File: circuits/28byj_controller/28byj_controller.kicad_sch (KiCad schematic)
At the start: 13 parts, among them J1 INPUT, J2 5V, M1 28BYJ-48_Stepper, M2 28BYJ-48_Stepper, U1 74HC595, U2 ULN2803A

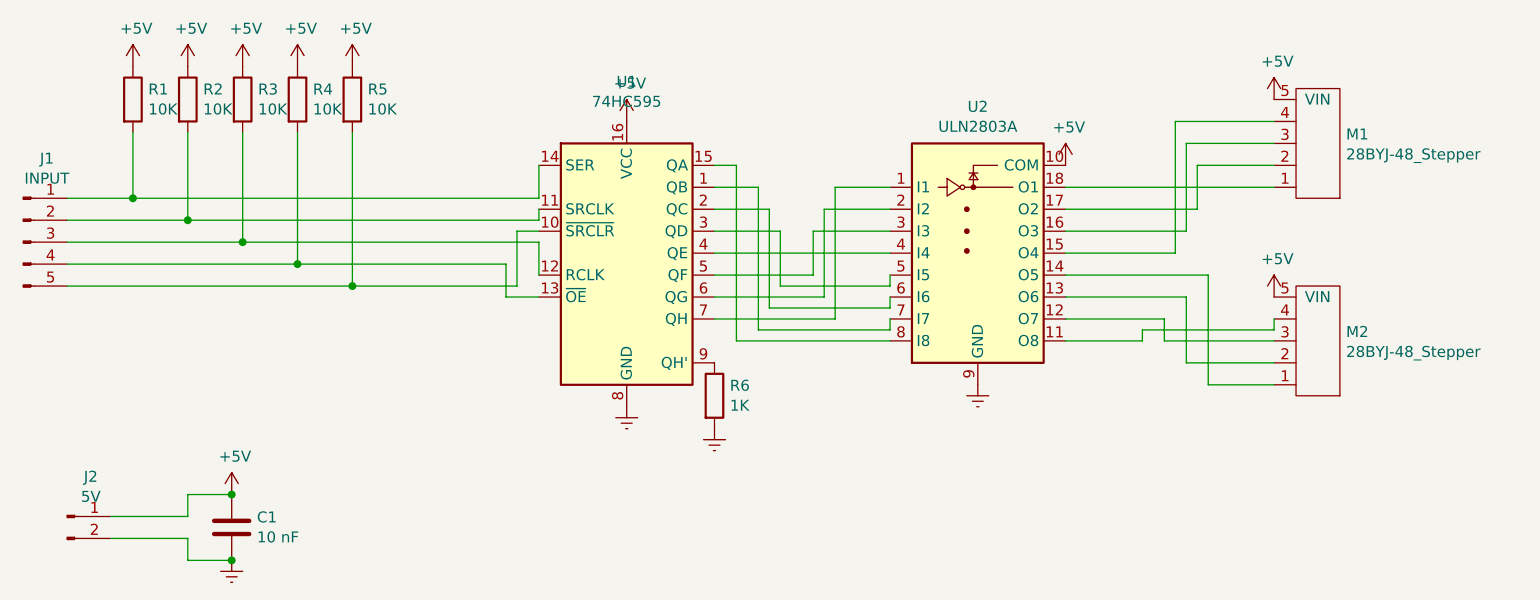
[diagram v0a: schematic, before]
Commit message: Code works and is tested on waveforms.
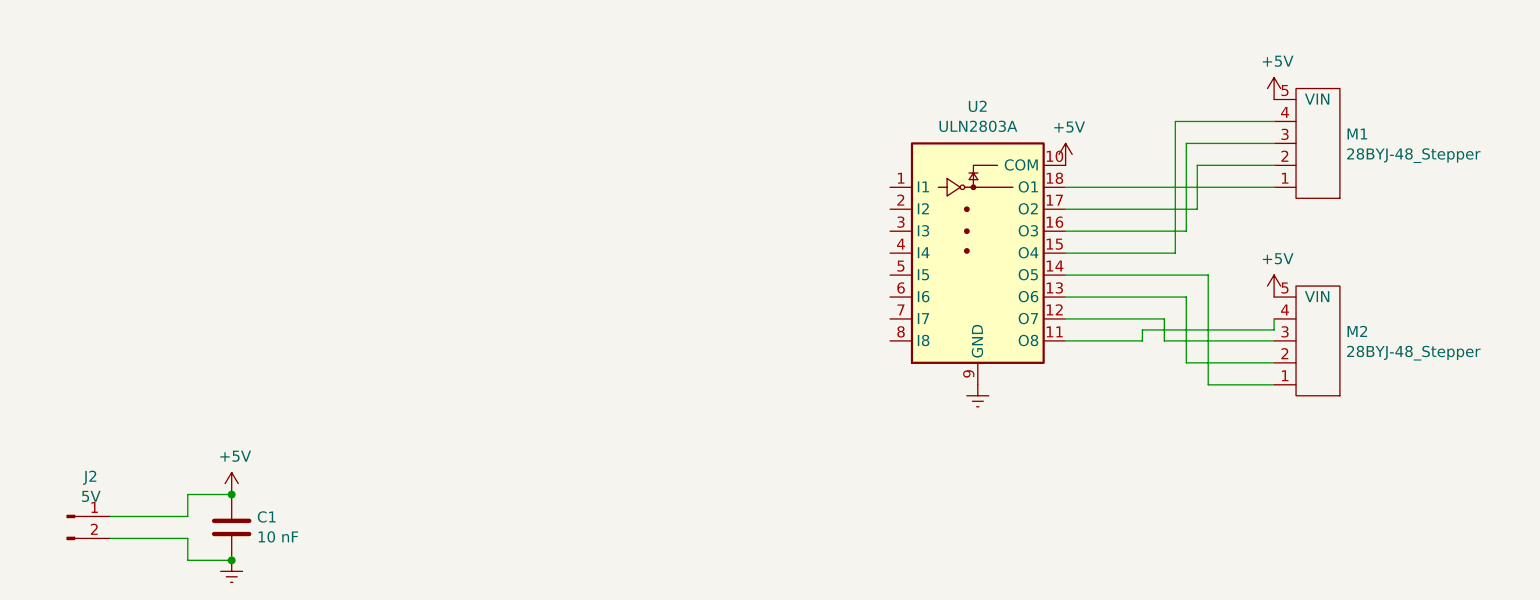
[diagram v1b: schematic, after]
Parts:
- removed J1: INPUT, Connector_JST:JST_XH_B5B-XH-A_1x05_P2.50mm_Vertical, symbol Connector:Conn_01x05_Male
- removed R1, R2, R3, R4, R5: 10K, Resistor_SMD:R_0805_2012Metric_Pad1.20x1.40mm_HandSolder, symbol Device:R
- removed R6: 1K, Resistor_SMD:R_0805_2012Metric_Pad1.20x1.40mm_HandSolder, symbol Device:R
- removed U1: 74HC595, Package_SO:SO-16_3.9x9.9mm_P1.27mm, symbol 74xx:74HC595
